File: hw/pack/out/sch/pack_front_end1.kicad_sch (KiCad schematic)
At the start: 17 parts, among them J1 3.5mm locking, U3 OPA1656

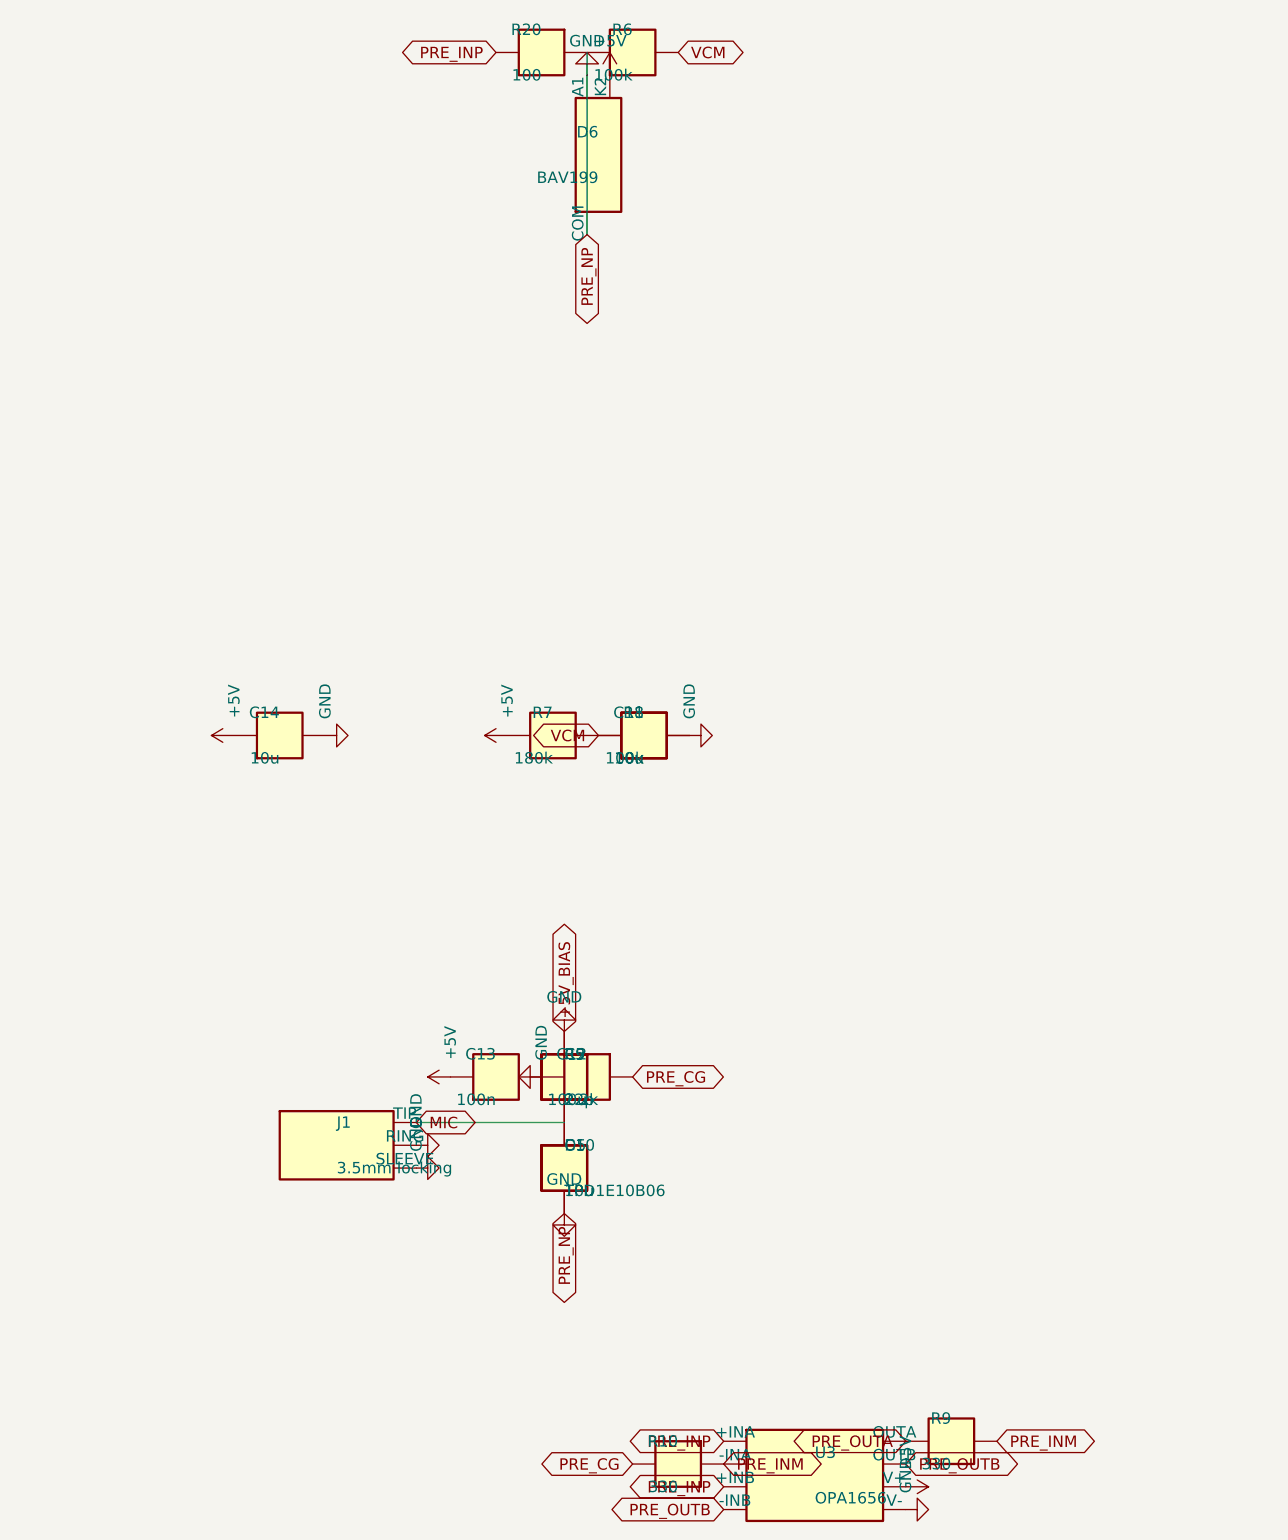
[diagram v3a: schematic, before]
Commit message: pack: cost-down to PK-12 $33.34: printed cell cradle + MYOUNG contacts, LCSC IPEX pigtail, priced M2 screws (#34)
- BT1: MYOUNG MY-18650-04-J/-05-J (LCSC C19184125/C19184124) in a printed
  cradle in the base (76 mm plate faces: spring 4.2-9.2 mm for 70-65 mm cells);
  the SMT BH-18650-B1BA002 holder is gone; footprint Cell_Wire_Pads
- pigtail: BAT Wireless BWIPX1-SMA-1.13L150 (LCSC C784404, $0.6015 @100), SMA
  cut off, ~100 mm + 31 mm wire whip; audit.py PIGTAIL_IL 0.46 <= 0.6 dB
- audit.py cutoff path includes the spring (0.10 ohm), cutoff stays 3.2 V
- 2 x M2x6 PT screws $0.112 (Fastener Superstore 585907)
- prices.py, bom.csv, pack_uk.csv (UK $34.81) updated

Co-Authored-By: Claude Opus 5.5 <noreply@anthropic.com>
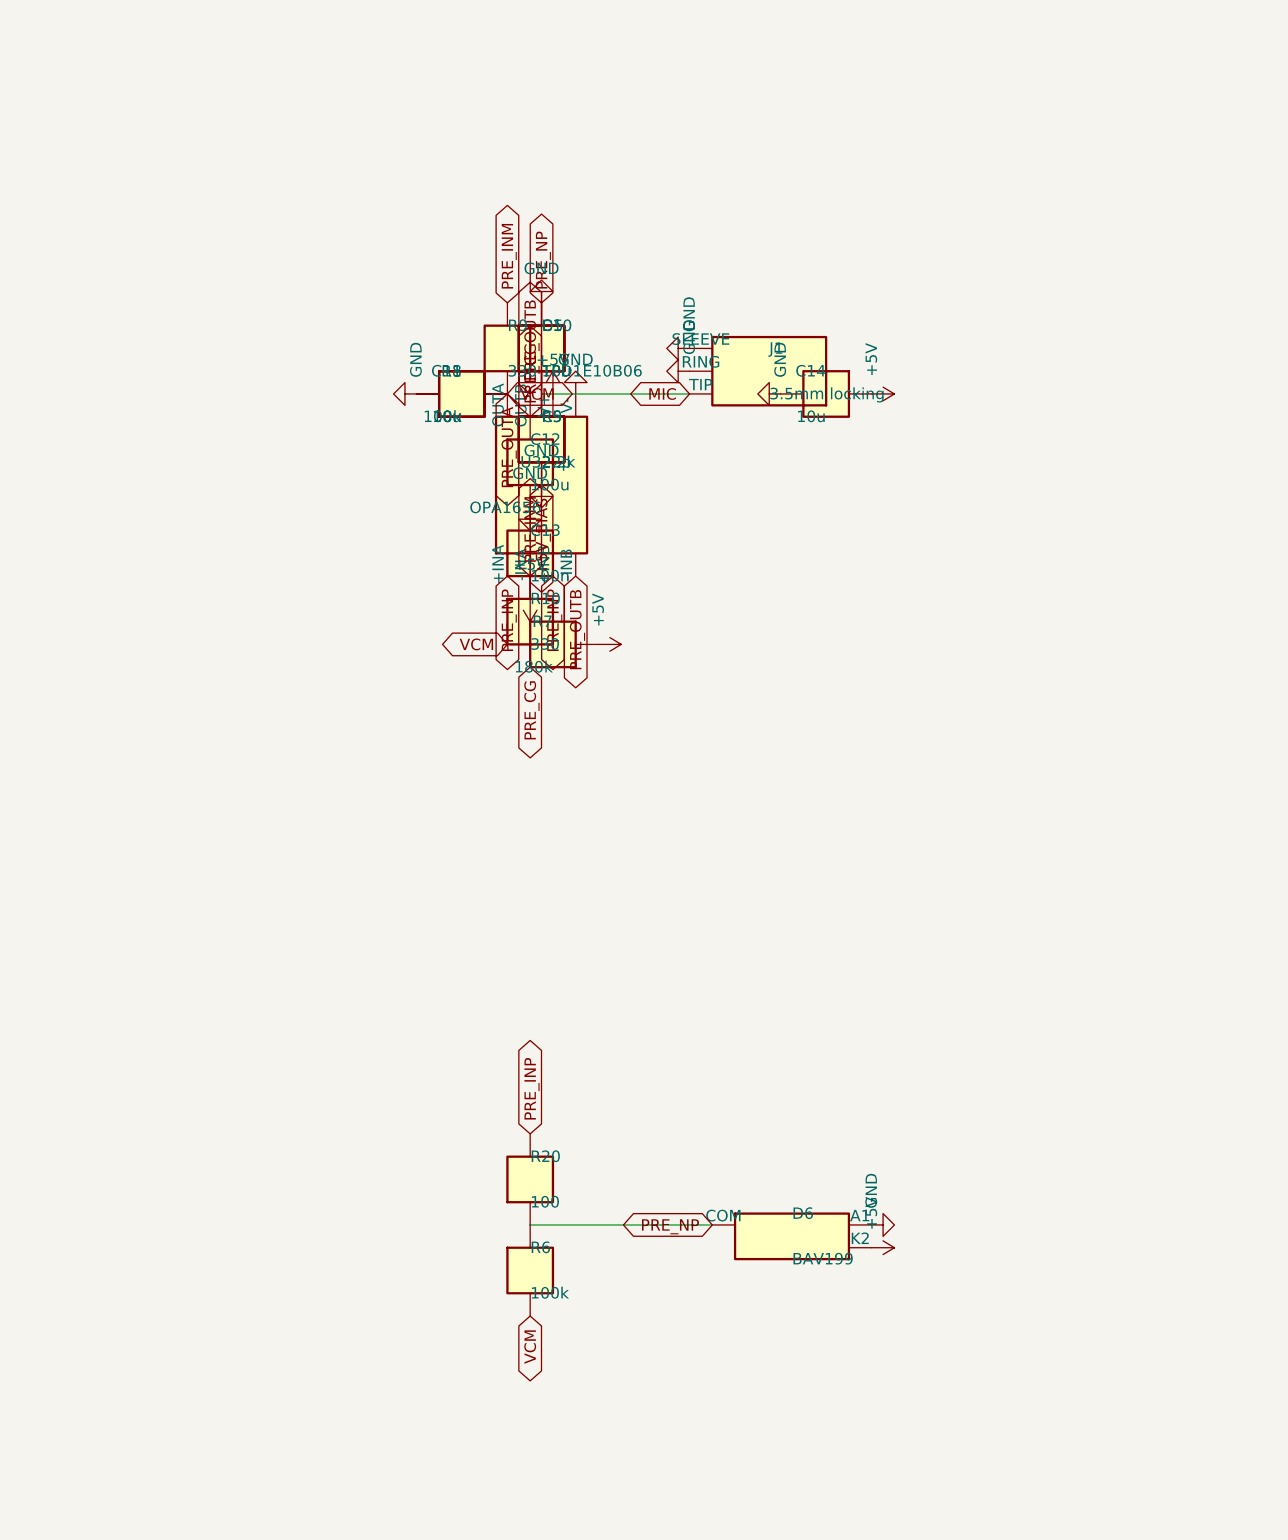
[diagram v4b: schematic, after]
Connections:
- net VCM is gone; now on net PRE_OUTA: C11.1, R6.2, R7.2, R8.1
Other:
- moved on the sheet: C10, C11, C12, C13, C14, C9, D5, D6, J1, R10, R20, R5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

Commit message: pack: #104 review fixes: 1 mm L1 battery path, test points, clip inserts off the antenna, pigtail route, JLC LCSC/rotations (#34)
- router: 'bat' class (1.0 mm, L1 only, necks <=1.36 mm at small pads);
  SW1 on-throw moved to pin 3 so feed and VSYS don't cross; 40 mOhm path
- audit.py: cell path from the board tracks (121 mOhm total, est. spring):
  cutoff computes 3.2012 V -> rounds to 3.3 V (reported, not tuned)
- TP3-TP11 folded in from review-104-tps (415194b), TP5/TP9-11 moved
- mech: clip inserts to (-24,3)/(-24,17) under the board; PIGTAIL route,
  bend radius, tie-down; fit.py checks both
- outputs: LCSC # per BOM line (verified), DNP/CONSIGN, CPL rotation table
- tests: battery path layer/width/R, BOM LCSC-or-DNP, rotation table

Co-Authored-By: Claude Opus 5.5 <noreply@anthropic.com>
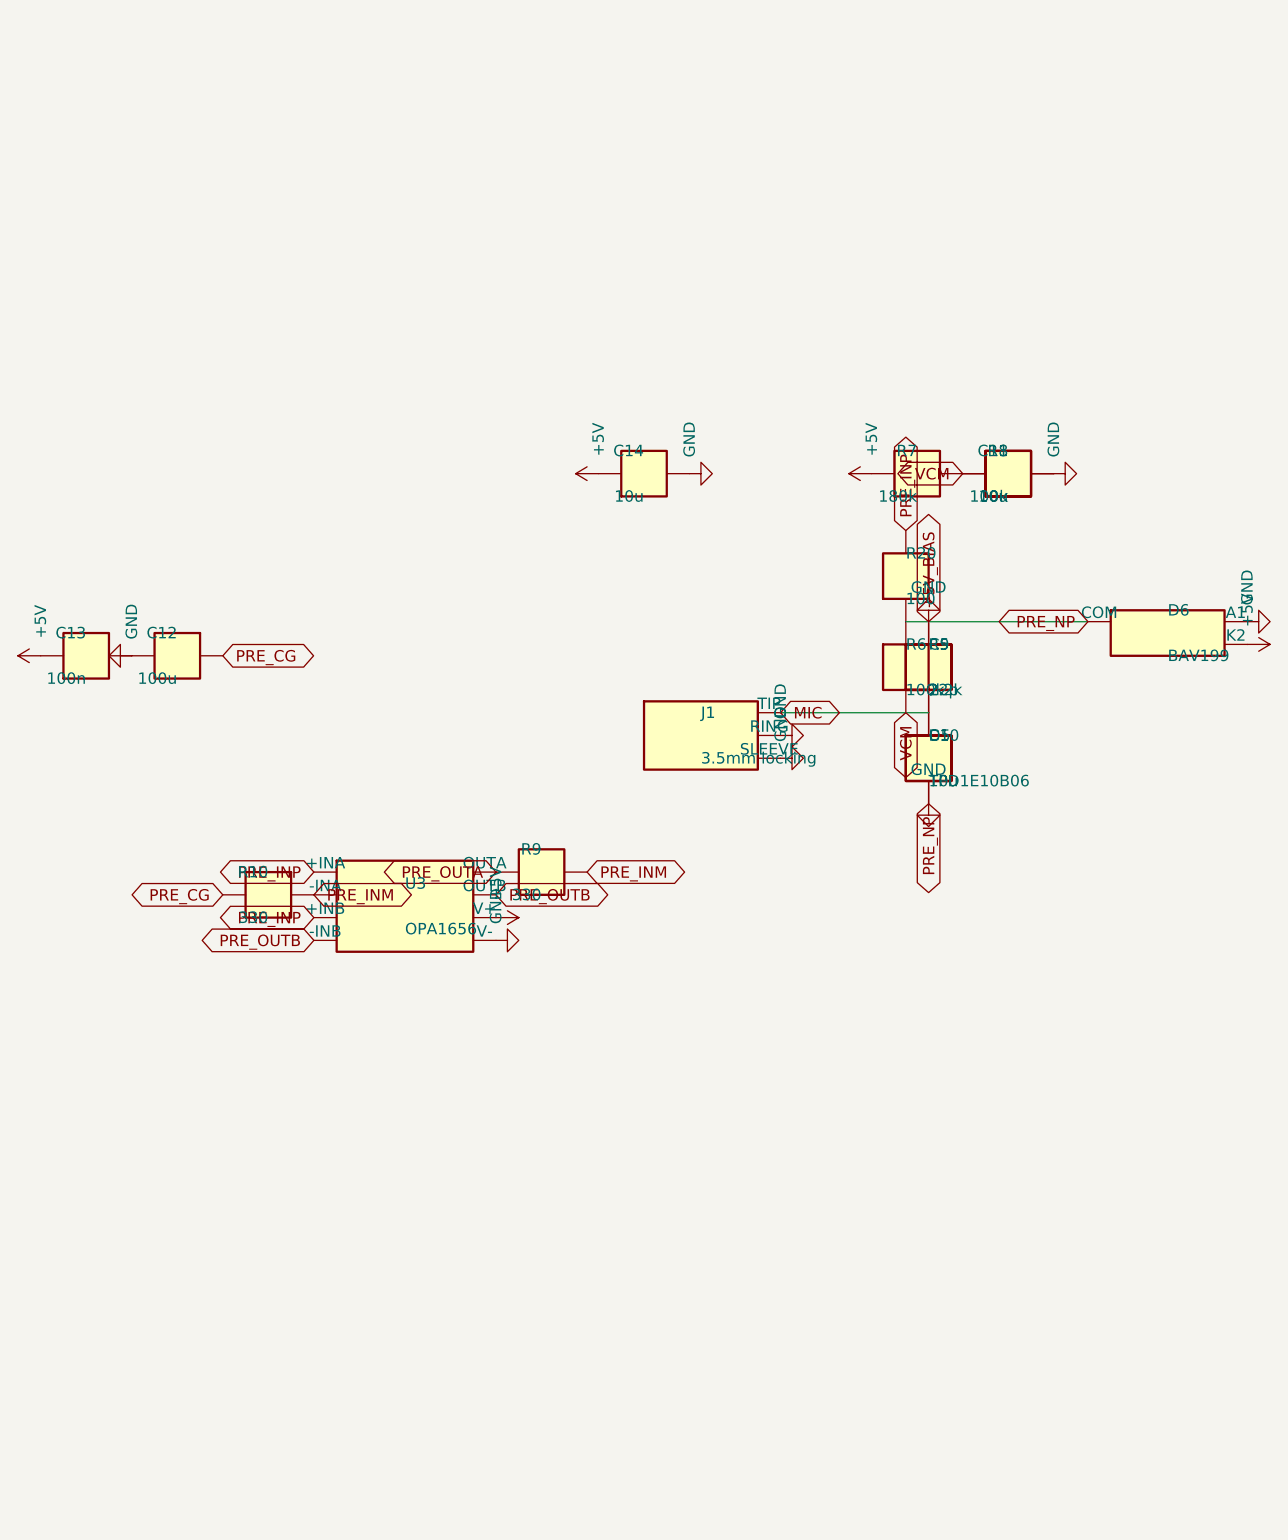
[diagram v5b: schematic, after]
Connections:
- net MIC: now also C11.1, R6.2, R7.2, R8.1
- net PRE_OUTA: no longer C11.1, R6.2, R7.2, R8.1
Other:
- moved on the sheet: C10, C11, C12, C13, C14, C9, D5, D6, J1, R10, R20, R5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
